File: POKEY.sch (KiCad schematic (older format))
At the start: 0 parts

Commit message: PIA and POKEY
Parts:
- added C69, C70: 100nF, Atari:C_Axial_L5.1mm_D2.5mm_P12.50mm_Horizontal, symbol Device:C
- added C75, C76, C77, C78: 1nF, Atari:C_Axial_L5.1mm_D2.5mm_P12.50mm_Horizontal, symbol Device:C
- added D5: 1N4148, Diode_THT:D_DO-35_SOD27_P12.70mm_Horizontal, symbol Diode:1N4148
- added R128, R129, R130, R131, R90: 100, Atari:R_Axial_DIN0207_L3.6mm_D2.2mm_P10.16mm_Horizontal, symbol Device:R
- added R137: 270, Atari:R_Axial_DIN0207_L3.6mm_D2.2mm_P10.16mm_Horizontal, symbol Device:R
- added R138, R139, R140, R141, R142, R143, R144, R145, R146, R147, R148, R149, R150, R151, R152, R153: 220, Atari:R_Axial_DIN0207_L3.6mm_D2.2mm_P10.16mm_Horizontal, symbol Device:R
- added R74, R75: 3k, Atari:R_Axial_DIN0207_L3.6mm_D2.2mm_P10.16mm_Horizontal, symbol Device:R
- added R80: 1k, Atari:R_Axial_DIN0207_L3.6mm_D2.2mm_P10.16mm_Horizontal, symbol Device:R
- added R81, R82, R83, R84: 4k7, Atari:R_Axial_DIN0207_L3.6mm_D2.2mm_P10.16mm_Horizontal, symbol Device:R
- added R89, R96: 47k, Atari:R_Axial_DIN0207_L3.6mm_D2.2mm_P10.16mm_Horizontal, symbol Device:R
- added U22: POKEY, Package_DIP:DIP-40_W15.24mm_Socket, symbol Atari:POKEY
- added U24, U25: CD4051B, Package_DIP:DIP-18_W7.62mm_Socket, symbol Analog_Switch:CD4051B
- added W1: 0, Atari:R_Axial_DIN0207_L3.6mm_D2.2mm_P10.16mm_Horizontal, symbol Device:R
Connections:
- new net: R75.1, U22.10 (P4), W1.1
- new net: D5.2 (A), R137.2, R96.1, U22.16 (~KR2)
- new net: R130.2, R83.2, U22.24 (SID)
- new net: R89.1, U22.25 (~KR1), U24.3 (X)
- new net: R129.2, R82.2, U22.26 (BCLK)
- new net: R128.2, R81.2, U22.27 (ACLK)
- new net: R131.2, R84.2, U22.28 (SOD)
- new net: R74.2, U22.31 (CS1)
- new net: R150.2, U24.1 (X4)
- new net: R149.2, U24.12 (X3)
- new net: R146.2, U24.13 (X0)
- new net: R147.2, U24.14 (X1)
- new net: R148.2, U24.15 (X2)
- new net: R152.2, U24.2 (X6)
- new net: R153.2, U24.4 (X7)
- new net: R151.2, U24.5 (X5)
- new net: R141.2, U25.1 (X4)
- new net: R142.2, U25.12 (X3)
- new net: R145.2, U25.13 (X0)
- new net: R144.2, U25.14 (X1)
- new net: R143.2, U25.15 (X2)
- new net: C70.1, U25.16 (VDD)
- new net: R139.2, U25.2 (X6)
- new net: R90.1, U25.3 (X)
- new net: R138.2, U25.4 (X7)
- new net: R140.2, U25.5 (X5)
- new net +5P: R80.2
- new net +5VA: C69.1, D5.1 (K), R74.1, R75.2, R81.1, R82.1, R83.1, R84.1, R89.2, R96.2, U24.16 (VDD)
- new net A0: U22.36 (A0)
- new net A1: U22.35 (A1)
- new net A2: U22.34 (A2)
- new net A3: U22.33 (A3)
- new net AUDIO: R80.1, U22.37 (AUDIO)
- new net BSC: R137.1
- new net CLK_IN: C76.1, R129.1
- new net CLK_OUT: C75.1, R128.1
- new net D0: U22.38 (D0)
- new net D1: U22.39 (D1)
- new net D2: U22.40 (D2)
- new net D3: U22.2 (D3)
- new net D4: U22.3 (D4)
- new net D5: U22.4 (D5)
- new net D6: U22.5 (D6)
- new net D7: U22.6 (D7)
- new net DATA_IN: C77.1, R130.1
- new net DATA_OUT: C78.1, R131.1
- new net GND: C69.2, C70.2, C75.2, C76.2, C77.2, C78.2, R90.2, U22.11 (P5), U22.8 (P6), U22.9 (P7), U24.6 (INH), U24.7 (VEE), U24.8 (VSS), U25.6 (INH), U25.7 (VEE), U25.8 (VSS), W1.2
- new net IN0: R146.1
- new net IN1: R147.1
- new net IN2: R148.1
- new net IN3: R149.1
- new net IN4: R150.1
- new net IN5: R151.1
- new net IN6: R152.1
- new net IN7: R153.1
- new net IRQ: U22.29 (~IRQ)
- new net K0: U22.23 (~K0), U24.9 (C)
- new net K1: U22.22 (~K1), U24.10 (B)
- new net K2: U22.21 (~K2), U24.11 (A)
- new net K3: U22.20 (~K3), U25.11 (A)
- new net K4: U22.19 (~K4), U25.10 (B)
- new net K5: U22.18 (~K5), U25.9 (C)
- new net O2: U22.7 (O2)
- new net OUT0: R145.1
- new net OUT1: R144.1
- new net OUT2: R143.1
- new net OUT3: R142.1
- new net OUT4: R141.1
- new net OUT5: R140.1
- new net OUT6: R139.1
- new net OUT7: R138.1
- new net POKEY: U22.30 (~CS0)
- new net RW: U22.32 (R/~W)

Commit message: Pokey finish
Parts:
- added C63, C64, C65, C66: 47nF, Atari:C_Axial_L5.1mm_D2.5mm_P12.50mm_Horizontal, symbol Device:C
- added C71, C72, C73, C74, C99: 1nF, Atari:C_Axial_L5.1mm_D2.5mm_P12.50mm_Horizontal, symbol Device:C
- added C98: 10uF, Capacitor_THT:CP_Radial_Tantal_D5.0mm_P2.50mm, symbol Device:CP
- added L15, L16, L17, L18, L24: 10uH, Atari:L_Axial_L7.0mm_D3.3mm_P12.50mm_Horizontal_Fastron_MICC, symbol Device:L
- added R76, R77, R78, R79: 1k8, Atari:R_Axial_DIN0207_L3.6mm_D2.2mm_P10.16mm_Horizontal, symbol Device:R
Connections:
- net +5P: now also U22.17 (VCC), C98.1, C99.1
- net GND: now also U22.1 (VSS), C63.2, C64.2, C65.2, C66.2, C71.2, C72.2, C73.2, C74.2, C98.2, C99.2, L24.2
- net at U22.12 (P2): now also C66.1, R79.2
- net at U22.13 (P3): now also C63.1, R78.2
- net at U22.14 (P0): now also C65.1, R77.2
- net at U22.15 (P1): now also C64.1, R76.2
- new net: C71.1, L17.2, R76.1
- new net: C72.1, L18.2, R77.1
- new net: C73.1, L15.2, R78.1
- new net: C74.1, L16.2, R79.1
- new net JOY_GND: L24.1
- new net POT_A0: L18.1
- new net POT_A1: L16.1
- new net POT_B0: L17.1
- new net POT_B1: L15.1

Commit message: Schema finished
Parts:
- removed L24: 10uH, Atari:L_Axial_L7.0mm_D3.3mm_P12.50mm_Horizontal_Fastron_MICC, symbol Device:L
- C98: footprint Capacitor_THT:CP_Radial_Tantal_D5.0mm_P2.50mm -> Capacitor_THT:C_Axial_L12.0mm_D6.5mm_P15.00mm_Horizontal
- U24, U25: footprint Package_DIP:DIP-18_W7.62mm_Socket -> Package_DIP:DIP-16_W7.62mm_Socket
- renumbered C99 to C62
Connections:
- net +5P: no longer R80.2
- net +5VA: now also C70.1, R80.2, U25.16 (VDD)
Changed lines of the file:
@@
 Wire Wire Line
 	2100 4250 1600 4250
-$Comp
-L power:+5P #PWR0220
-U 1 1 603F705D
-P 825 3825
-F 0 "#PWR0220" H 825 3675 50  0001 C CNN
-F 1 "+5P" H 840 3998 50  0000 C CNN
-F 2 "" H 825 3825 50  0001 C CNN
-F 3 "" H 825 3825 50  0001 C CNN
-	1    825  3825
-	1    0    0    -1
-$EndComp
 Wire Wire Line
 	1125 4250 825  4250
@@
 F 0 "U24" H 8225 2500 50  0000 C CNN
 F 1 "CD4051B" H 8800 2500 50  0000 C CNN
-F 2 "Package_DIP:DIP-18_W7.62mm_Socket" H 8675 1100 50  0001 L CNN
+F 2 "Package_DIP:DIP-16_W7.62mm_Socket" H 8675 1100 50  0001 L CNN
 F 3 "http://www.ti.com/lit/ds/symlink/cd4052b.pdf" H 8505 1950 50  0001 C CNN
 	1    8525 1850
@@
 F 0 "U25" H 8225 4500 50  0000 C CNN
 F 1 "CD4051B" H 8800 4500 50  0000 C CNN
-F 2 "Package_DIP:DIP-18_W7.62mm_Socket" H 8675 3100 50  0001 L CNN
+F 2 "Package_DIP:DIP-16_W7.62mm_Socket" H 8675 3100 50  0001 L CNN
 F 3 "http://www.ti.com/lit/ds/symlink/cd4052b.pdf" H 8505 3950 50  0001 C CNN
 	1    8525 3850
@@
 Connection ~ 5675 5700
 $Comp
-L power:GND #PWR?
+L power:GND #PWR0231
 U 1 1 60348277
 P 5675 5850
-F 0 "#PWR?" H 5675 5600 50  0001 C CNN
+F 0 "#PWR0231" H 5675 5600 50  0001 C CNN
 F 1 "GND" H 5800 5825 50  0000 C CNN
 F 2 "" H 5675 5850 50  0001 C CNN
@@
 Connection ~ 8225 6250
 $Comp
-L power:GND #PWR?
+L power:GND #PWR0232
 U 1 1 603A068D
 P 8225 6350
-F 0 "#PWR?" H 8225 6100 50  0001 C CNN
+F 0 "#PWR0232" H 8225 6100 50  0001 C CNN
 F 1 "GND" H 8350 6325 50  0000 C CNN
 F 2 "" H 8225 6350 50  0001 C CNN
@@
 	8225 6250 8225 6350
 $Comp
-L Device:C C99
+L Device:C C62
 U 1 1 603B0EE9
 P 3675 4650
-F 0 "C99" H 3700 4725 50  0000 L CNN
+F 0 "C62" H 3700 4725 50  0000 L CNN
 F 1 "1nF" H 3700 4575 50  0000 L CNN
 F 2 "Atari:C_Axial_L5.1mm_D2.5mm_P12.50mm_Horizontal" H 3713 4500 50  0001 C CNN
@@
 F 0 "C98" H 4168 4696 50  0000 L CNN
 F 1 "10uF" H 4168 4605 50  0000 L CNN
-F 2 "Capacitor_THT:CP_Radial_Tantal_D5.0mm_P2.50mm" H 4088 4500 50  0001 C CNN
+F 2 "Capacitor_THT:C_Axial_L12.0mm_D6.5mm_P15.00mm_Horizontal" H 4088 4500 50  0001 C CNN
 F 3 "~" H 4050 4650 50  0001 C CNN
 	1    4050 4650
@@
 Connection ~ 3675 4800
 $Comp
-L power:+5P #PWR?
+L power:+5P #PWR0233
 U 1 1 603D3936
 P 4375 4500
-F 0 "#PWR?" H 4375 4350 50  0001 C CNN
+F 0 "#PWR0233" H 4375 4350 50  0001 C CNN
 F 1 "+5P" H 4450 4550 50  0000 C CNN
 F 2 "" H 4375 4500 50  0001 C CNN
@@
 Connection ~ 4050 4500
 $Comp
-L power:GND #PWR?
+L power:GND #PWR0234
 U 1 1 603DD0C0
 P 3300 4950
-F 0 "#PWR?" H 3300 4700 50  0001 C CNN
+F 0 "#PWR0234" H 3300 4700 50  0001 C CNN
 F 1 "GND" H 3425 4925 50  0000 C CNN
 F 2 "" H 3300 4950 50  0001 C CNN
@@
 Connection ~ 3300 4800
 $Comp
-L Device:L L24
-U 1 1 603E6BD7
-P 4475 4800
-F 0 "L24" V 4550 4800 50  0000 C CNN
-F 1 "10uH" V 4425 4800 50  0000 C CNN
-F 2 "Atari:L_Axial_L7.0mm_D3.3mm_P12.50mm_Horizontal_Fastron_MICC" H 4475 4800 50  0001 C CNN
-F 3 "~" H 4475 4800 50  0001 C CNN
-	1    4475 4800
-	0    1    1    0
-$EndComp
-Wire Wire Line
-	4050 4800 4325 4800
-Connection ~ 4050 4800
-Text GLabel 4625 4800 2    50   Input ~ 0
-JOY_GND
+L power:+5VA #PWR0220
+U 1 1 60329E83
+P 825 3825
+F 0 "#PWR0220" H 825 3675 50  0001 C CNN
+F 1 "+5VA" H 840 3998 50  0000 C CNN
+F 2 "" H 825 3825 50  0001 C CNN
+F 3 "" H 825 3825 50  0001 C CNN
+	1    825  3825
+	1    0    0    -1
+$EndComp
+$Comp
+L power:+5VA #PWR0237
+U 1 1 6033E627
+P 9375 2725
+F 0 "#PWR0237" H 9375 2575 50  0001 C CNN
+F 1 "+5VA" H 9390 2898 50  0000 C CNN
+F 2 "" H 9375 2725 50  0001 C CNN
+F 3 "" H 9375 2725 50  0001 C CNN
+	1    9375 2725
+	1    0    0    -1
+$EndComp
+Wire Wire Line
+	9375 2725 9375 2850
+Connection ~ 9375 2850
 $EndSCHEMATC

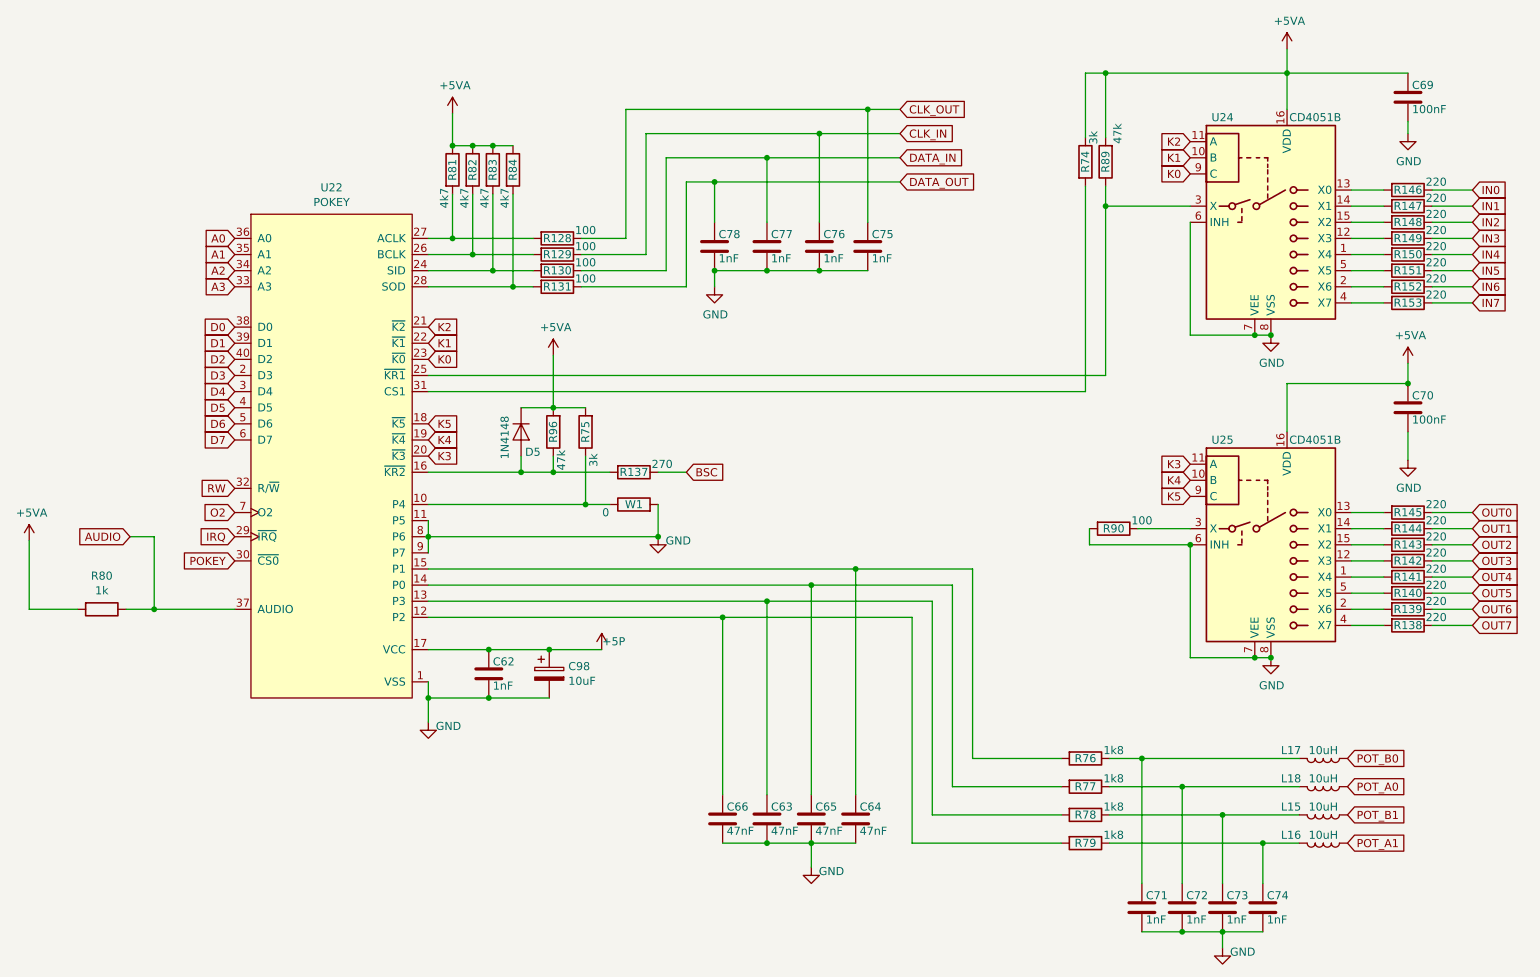
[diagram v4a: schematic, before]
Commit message: Audio put on board
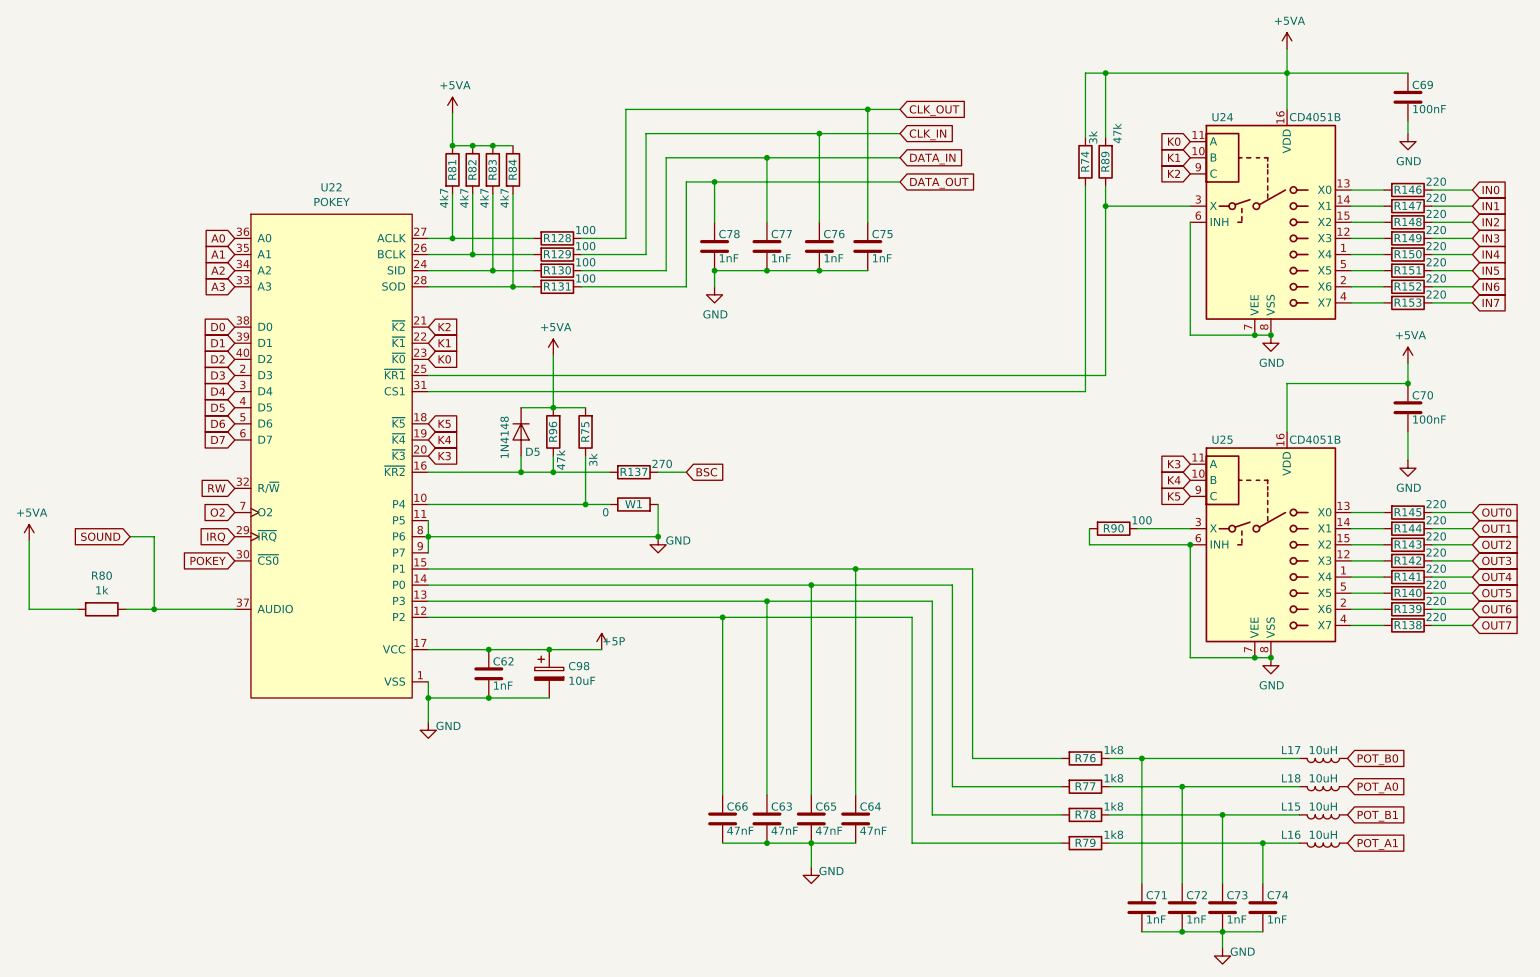
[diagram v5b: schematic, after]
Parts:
- C98: footprint Capacitor_THT:C_Axial_L12.0mm_D6.5mm_P15.00mm_Horizontal -> Capacitor_THT:CP_Axial_L11.0mm_D6.0mm_P18.00mm_Horizontal
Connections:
- net K0: now also U24.11 (A); no longer U24.9 (C)
- net K2: now also U24.9 (C); no longer U24.11 (A)
- net AUDIO renamed SOUND
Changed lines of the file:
@@
 	825  4250 825  3825
 Text GLabel 1450 3800 0    50   Input ~ 0
-AUDIO
+SOUND
 Wire Wire Line
 	1450 3800 1600 3800
@@
 Text GLabel 3300 3300 2    50   Input ~ 0
 K3
-Text GLabel 8025 1350 0    50   Input ~ 0
+Text GLabel 8025 1550 0    50   Input ~ 0
 K2
 Text GLabel 8025 1450 0    50   Input ~ 0
 K1
-Text GLabel 8025 1550 0    50   Input ~ 0
+Text GLabel 8025 1350 0    50   Input ~ 0
 K0
 Wire Wire Line
@@
 F 0 "C98" H 4168 4696 50  0000 L CNN
 F 1 "10uF" H 4168 4605 50  0000 L CNN
-F 2 "Capacitor_THT:C_Axial_L12.0mm_D6.5mm_P15.00mm_Horizontal" H 4088 4500 50  0001 C CNN
+F 2 "Capacitor_THT:CP_Axial_L11.0mm_D6.0mm_P18.00mm_Horizontal" H 4088 4500 50  0001 C CNN
 F 3 "~" H 4050 4650 50  0001 C CNN
 	1    4050 4650

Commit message: Patching
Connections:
- net O2 renamed BO2
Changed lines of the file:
@@
 RW
 Text GLabel 2100 3650 0    50   Input ~ 0
-O2
+BO2
 Text GLabel 2100 3800 0    50   Input ~ 0
 IRQ

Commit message: Gerber and Tracking
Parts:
- added J108, J109, J110, J111: pin, Connector_PinHeader_2.00mm:PinHeader_1x01_P2.00mm_Vertical, symbol Connector_Generic:Conn_01x01
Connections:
- net GND: now also J108.1 (Pin_1), J109.1 (Pin_1), J110.1 (Pin_1), J111.1 (Pin_1)
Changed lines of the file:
@@
 Wire Wire Line
 	5125 5700 5400 5700
-Wire Wire Line
-	5400 5700 5675 5700
 Connection ~ 5400 5700
 Wire Wire Line
@@
 L power:GND #PWR0231
 U 1 1 60348277
-P 5675 5850
-F 0 "#PWR0231" H 5675 5600 50  0001 C CNN
-F 1 "GND" H 5800 5825 50  0000 C CNN
-F 2 "" H 5675 5850 50  0001 C CNN
-F 3 "" H 5675 5850 50  0001 C CNN
-	1    5675 5850
-	1    0    0    -1
-$EndComp
-Wire Wire Line
-	5675 5700 5675 5850
+P 4775 5925
+F 0 "#PWR0231" H 4775 5675 50  0001 C CNN
+F 1 "GND" H 4900 5900 50  0000 C CNN
+F 2 "" H 4775 5925 50  0001 C CNN
+F 3 "" H 4775 5925 50  0001 C CNN
+	1    4775 5925
+	1    0    0    -1
+$EndComp
 $Comp
 L Device:L L17
@@
 	9375 2725 9375 2850
 Connection ~ 9375 2850
+$Comp
+L Connector_Generic:Conn_01x01 J108
+U 1 1 60481C84
+P 5125 6025
+F 0 "J108" V 4997 6105 50  0000 L CNN
+F 1 "pin" V 5088 6105 50  0000 L CNN
+F 2 "Connector_PinHeader_2.00mm:PinHeader_1x01_P2.00mm_Vertical" H 5125 6025 50  0001 C CNN
+F 3 "~" H 5125 6025 50  0001 C CNN
+	1    5125 6025
+	0    1    1    0
+$EndComp
+Wire Wire Line
+	5125 5825 5125 5700
+Connection ~ 5125 5700
+Wire Wire Line
+	5125 5700 4775 5700
+Wire Wire Line
+	4775 5700 4775 5925
+$Comp
+L Connector_Generic:Conn_01x01 J109
+U 1 1 604990D0
+P 5400 6025
+F 0 "J109" V 5272 6105 50  0000 L CNN
+F 1 "pin" V 5363 6105 50  0000 L CNN
+F 2 "Connector_PinHeader_2.00mm:PinHeader_1x01_P2.00mm_Vertical" H 5400 6025 50  0001 C CNN
+F 3 "~" H 5400 6025 50  0001 C CNN
+	1    5400 6025
+	0    1    1    0
+$EndComp
+$Comp
+L Connector_Generic:Conn_01x01 J110
+U 1 1 604995D3
+P 5675 6025
+F 0 "J110" V 5547 6105 50  0000 L CNN
+F 1 "pin" V 5638 6105 50  0000 L CNN
+F 2 "Connector_PinHeader_2.00mm:PinHeader_1x01_P2.00mm_Vertical" H 5675 6025 50  0001 C CNN
+F 3 "~" H 5675 6025 50  0001 C CNN
+	1    5675 6025
+	0    1    1    0
+$EndComp
+$Comp
+L Connector_Generic:Conn_01x01 J111
+U 1 1 604998EB
+P 5950 6025
+F 0 "J111" V 5822 6105 50  0000 L CNN
+F 1 "pin" V 5913 6105 50  0000 L CNN
+F 2 "Connector_PinHeader_2.00mm:PinHeader_1x01_P2.00mm_Vertical" H 5950 6025 50  0001 C CNN
+F 3 "~" H 5950 6025 50  0001 C CNN
+	1    5950 6025
+	0    1    1    0
+$EndComp
+Wire Wire Line
+	5400 5825 5400 5700
+Wire Wire Line
+	5675 5825 5675 5700
+Wire Wire Line
+	5400 5700 5675 5700
+Wire Wire Line
+	5950 5825 5950 5700
+Connection ~ 5950 5700
 $EndSCHEMATC

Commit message: Trackimg
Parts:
- added J201: Diagnostic, Connector_PinHeader_2.54mm:PinHeader_1x04_P2.54mm_Vertical, symbol Connector_Generic:Conn_01x04
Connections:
- net CLK_IN: now also J201.1 (Pin_1)
- net CLK_OUT: now also J201.2 (Pin_2)
- net DATA_IN: now also J201.3 (Pin_3)
- net DATA_OUT: now also J201.4 (Pin_4)
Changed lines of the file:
@@
 	5950 5825 5950 5700
 Connection ~ 5950 5700
+$Comp
+L Connector_Generic:Conn_01x04 J201
+U 1 1 604341BE
+P 2425 6050
+F 0 "J201" H 2505 6042 50  0000 L CNN
+F 1 "Diagnostic" H 2505 5951 50  0000 L CNN
+F 2 "Connector_PinHeader_2.54mm:PinHeader_1x04_P2.54mm_Vertical" H 2425 6050 50  0001 C CNN
+F 3 "~" H 2425 6050 50  0001 C CNN
+	1    2425 6050
+	1    0    0    -1
+$EndComp
+Text GLabel 2225 6050 0    50   Input ~ 0
+CLK_OUT
+Text GLabel 2225 5950 0    50   Input ~ 0
+CLK_IN
+Text GLabel 2225 6150 0    50   Input ~ 0
+DATA_IN
+Text GLabel 2225 6250 0    50   Input ~ 0
+DATA_OUT
 $EndSCHEMATC
